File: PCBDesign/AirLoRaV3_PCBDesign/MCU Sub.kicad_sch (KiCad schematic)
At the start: 16 parts, among them SW3 SW_Push, U5 STM32F103C8Tx, Y2 8Mhz

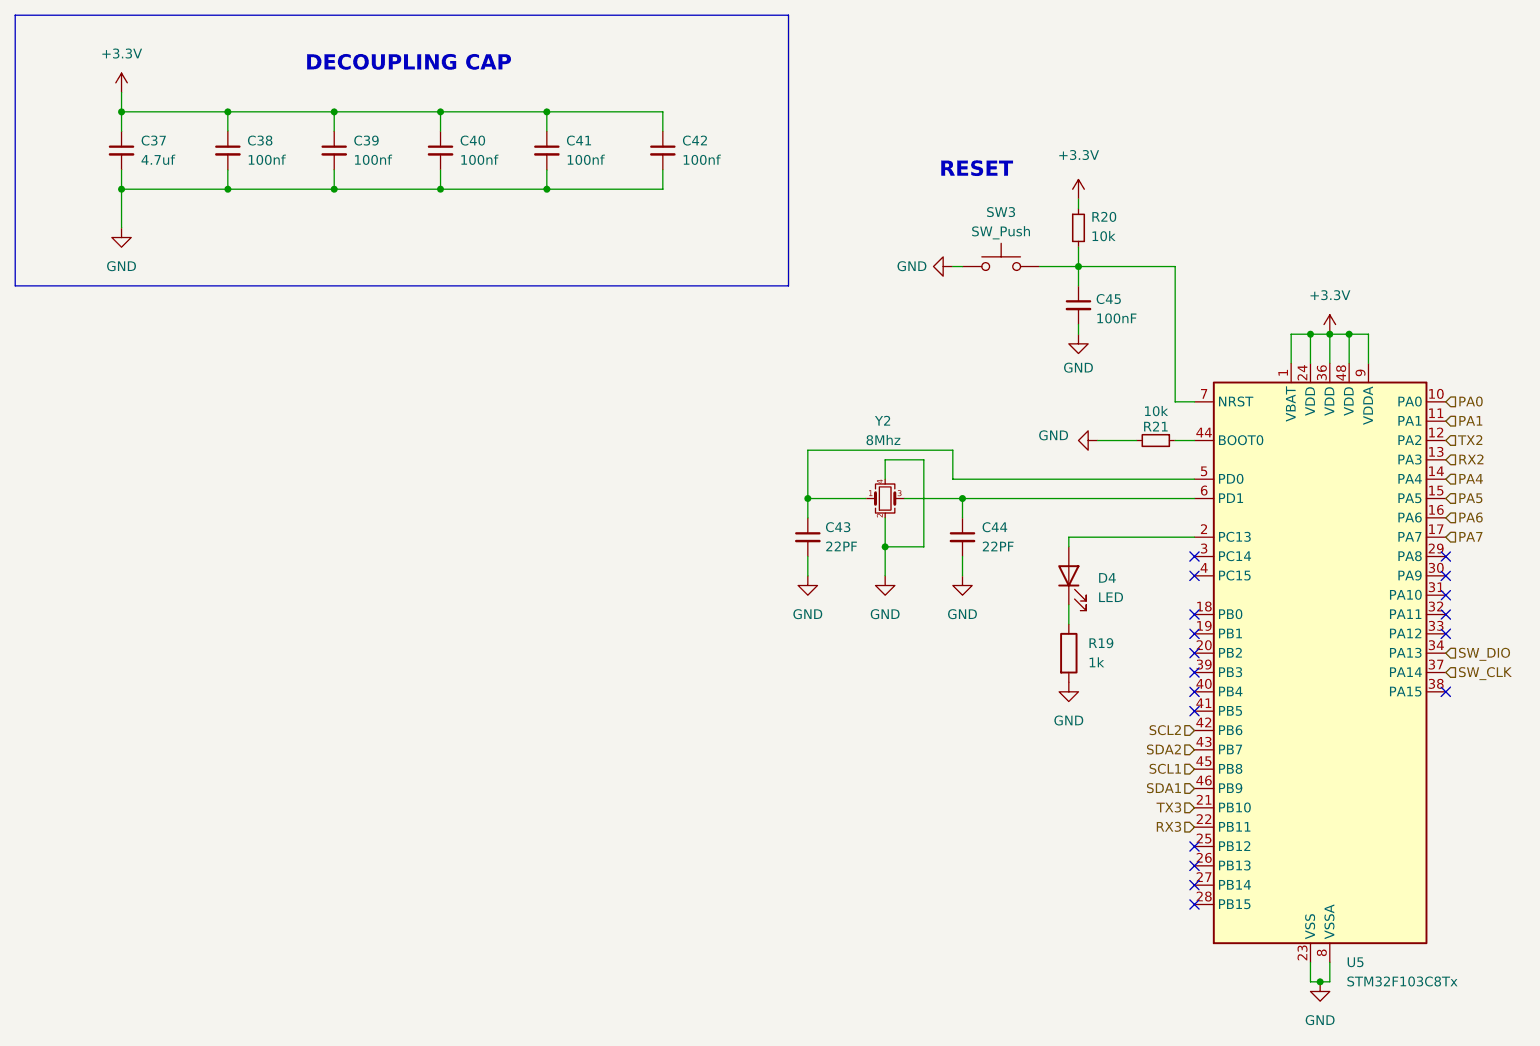
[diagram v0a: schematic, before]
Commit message: Update circuit buck converter and sensor
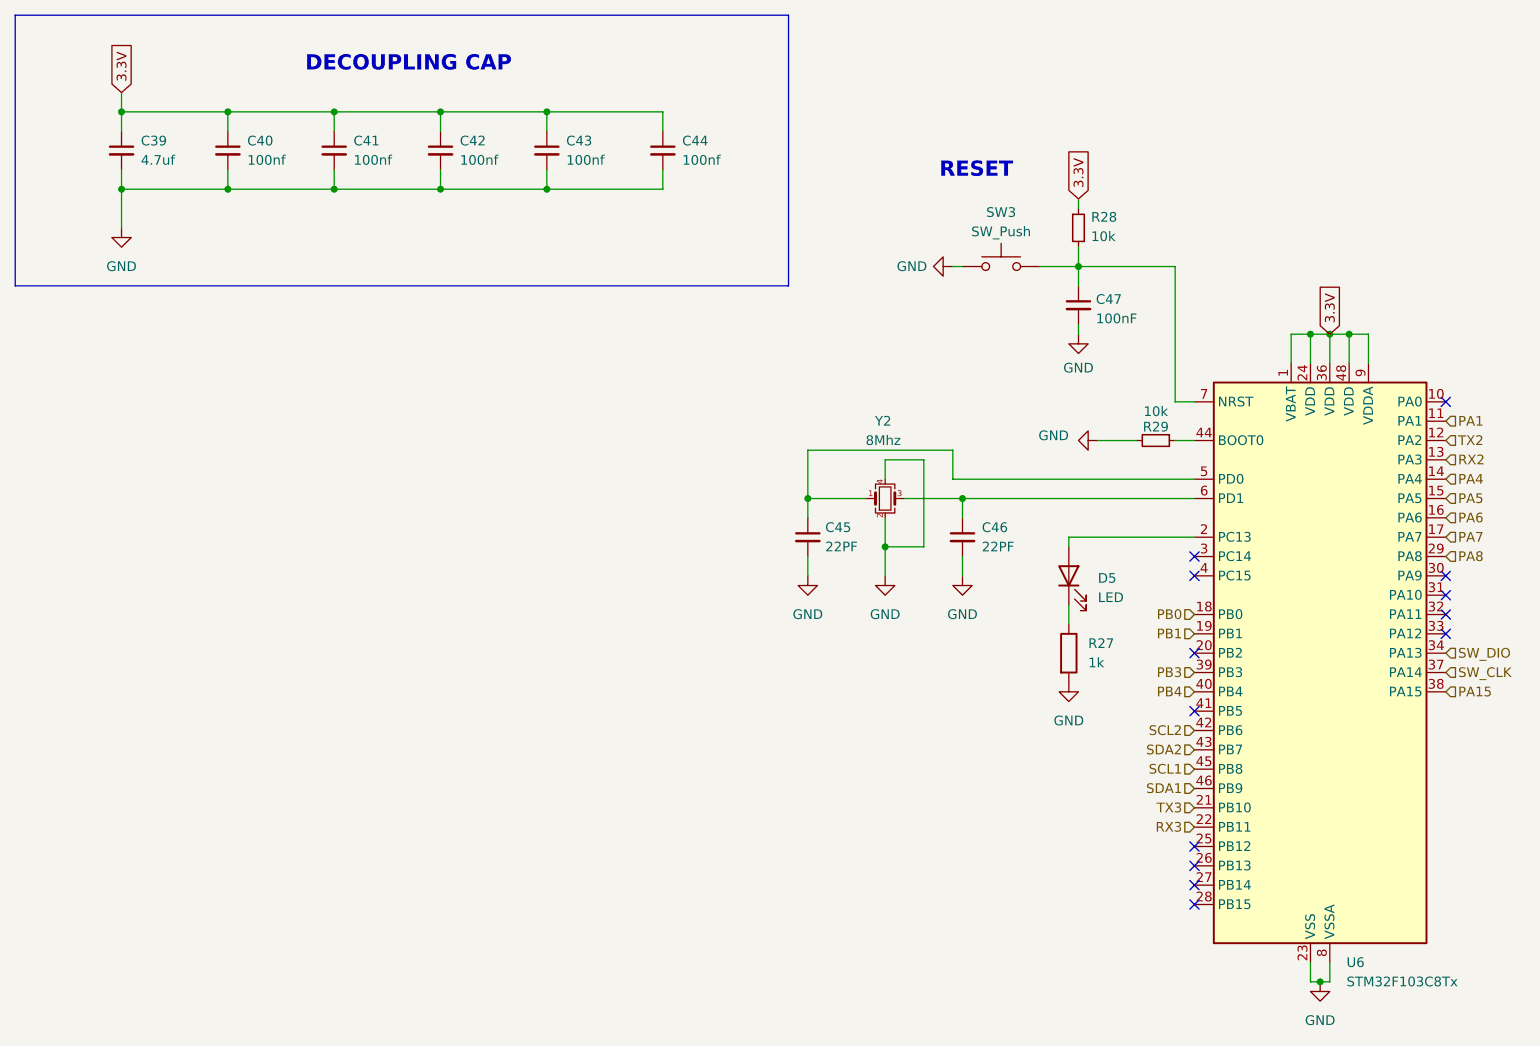
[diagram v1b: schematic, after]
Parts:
- renumbered C37 to C39, C38 to C40, C39 to C41, C40 to C42, C41 to C43, C42 to C44, C43 to C45, C44 to C46, C45 to C47, D4 to D5, R19 to R27, R20 to R28, R21 to R29, U5 to U6
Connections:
- net PB0: now reaches U6.18 (PB0)
- net PB1: now reaches U6.19 (PB1)
- net PA8: now reaches U6.29 (PA8)
- net PA15: now reaches U6.38 (PA15)
- net PB3: now reaches U6.39 (PB3)
- net PB4: now reaches U6.40 (PB4)
- net +3.3V renamed 3.3V
- net PA0: no longer names the net of U6.10 (PA0)
- no-connect marks 18 -> 13

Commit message: Update schematic
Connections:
- net 3.3V renamed +3.3V_HP
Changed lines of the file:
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@@
-		)
-	)
-	(global_label "3.3V"
-		(shape input)
-		(at 29.21 26.67 90)
-		(fields_autoplaced yes)
-		(effects
-			(font
-				(size 1.27 1.27)
-			)
-			(justify left)
-		)
-		(property "Intersheetrefs" "${INTERSHEET_REFS}"
-			(at 29.21 19.5724 90)
-			(effects
-				(font
-					(size 1.27 1.27)
-				)
-				(justify left)
-				(hide yes)
-			)
-		)
-	)
-	(global_label "3.3V"
-		(shape input)
-		(at 187.96 58.42 90)
-		(fields_autoplaced yes)
-		(effects
-			(font
-				(size 1.27 1.27)
-			)
-			(justify left)
-		)
-		(property "Intersheetrefs" "${INTERSHEET_REFS}"
-			(at 187.96 51.3224 90)
-			(effects
-				(font
-					(size 1.27 1.27)
-				)
-				(justify left)
-				(hide yes)
-			)
-		)
-	)
-	(global_label "3.3V"
-		(shape input)
-		(at 154.94 40.64 90)
-		(fields_autoplaced yes)
-		(effects
-			(font
-				(size 1.27 1.27)
-			)
-			(justify left)
-		)
-		(property "Intersheetrefs" "${INTERSHEET_REFS}"
-			(at 154.94 33.5424 90)
-			(effects
-				(font
-					(size 1.27 1.27)
-				)
-				(justify left)
-				(hide yes)
-			)
 		)
 	)
@@
 	)
 	(symbol
+		(lib_id "power:+3.3V")
+		(at 154.94 40.64 0)
+		(unit 1)
+		(exclude_from_sim no)
+		(in_bom yes)
+		(on_board yes)
+		(dnp no)
+		(fields_autoplaced yes)
+		(property "Reference" "#PWR068"
+			(at 154.94 44.45 0)
+			(effects
+				(font
+					(size 1.27 1.27)
+				)
+				(hide yes)
+			)
+		)
+		(property "Value" "+3.3V_HP"
+			(at 154.94 35.56 0)
+			(effects
+				(font
+					(size 1.27 1.27)
+				)
+			)
+		)
+		(property "Footprint" ""
+			(at 154.94 40.64 0)
+			(effects
+				(font
+					(size 1.27 1.27)
+				)
+				(hide yes)
+			)
+		)
+		(property "Datasheet" ""
+			(at 154.94 40.64 0)
+			(effects
+				(font
+					(size 1.27 1.27)
+				)
+				(hide yes)
+			)
+		)
+		(property "Description" "Power symbol creates a global label with name \"+3.3V\""
+			(at 154.94 40.64 0)
+			(effects
+				(font
+					(size 1.27 1.27)
+				)
+				(hide yes)
+			)
+		)
+		(pin "1"
+		)
+		(instances
+			(project "airlora-kicad"
+				(path "/59d971df-d6c1-4ef7-a085-bf08b7b16047/be77b740-d58b-414b-97ce-61f1d1685314/eab4a250-4bd5-4f82-b1cd-88a390e22a6b"
+					(reference "#PWR068")
+					(unit 1)
+				)
+			)
+		)
+	)
+	(symbol
 		(lib_id "power:GND")
 		(at 139.7 90.17 0)
@@
 	)
 	(symbol
+		(lib_id "power:+3.3V")
+		(at 187.96 58.42 0)
+		(unit 1)
+		(exclude_from_sim no)
+		(in_bom yes)
+		(on_board yes)
+		(dnp no)
+		(fields_autoplaced yes)
+		(property "Reference" "#PWR069"
+			(at 187.96 62.23 0)
+			(effects
+				(font
+					(size 1.27 1.27)
+				)
+				(hide yes)
+			)
+		)
+		(property "Value" "+3.3V_HP"
+			(at 187.96 53.34 0)
+			(effects
+				(font
+					(size 1.27 1.27)
+				)
+			)
+		)
+		(property "Footprint" ""
+			(at 187.96 58.42 0)
+			(effects
+				(font
+					(size 1.27 1.27)
+				)
+				(hide yes)
+			)
+		)
+		(property "Datasheet" ""
+			(at 187.96 58.42 0)
+			(effects
+				(font
+					(size 1.27 1.27)
+				)
+				(hide yes)
+			)
+		)
+		(property "Description" "Power symbol creates a global label with name \"+3.3V\""
+			(at 187.96 58.42 0)
+			(effects
+				(font
+					(size 1.27 1.27)
+				)
+				(hide yes)
+			)
+		)
+		(pin "1"
+		)
+		(instances
+			(project "airlora-kicad"
+				(path "/59d971df-d6c1-4ef7-a085-bf08b7b16047/be77b740-d58b-414b-97ce-61f1d1685314/eab4a250-4bd5-4f82-b1cd-88a390e22a6b"
+					(reference "#PWR069")
+					(unit 1)
+				)
+			)
+		)
+	)
+	(symbol
 		(lib_id "Device:C_Small")
 		(at 85.09 34.29 0)
@@
 					(unit 1)
 				)
+			)
+		)
+	)
+	(symbol
+		(lib_id "power:+3.3V")
+		(at 29.21 26.67 0)
+		(unit 1)
+		(exclude_from_sim no)
+		(in_bom yes)
+		(on_board yes)
+		(dnp no)
+		(fields_autoplaced yes)
+		(property "Reference" "#PWR070"
+			(at 29.21 30.48 0)
+			(effects
+				(font
+					(size 1.27 1.27)
+				)
+				(hide yes)
+			)
+		)
+		(property "Value" "+3.3V_HP"
+			(at 29.21 21.59 0)
+			(effects
+				(font
+					(size 1.27 1.27)
+				)
+			)
+		)
+		(property "Footprint" ""
+			(at 29.21 26.67 0)
+			(effects
+				(font
+					(size 1.27 1.27)
+				)
+				(hide yes)
+			)
+		)
+		(property "Datasheet" ""
+			(at 29.21 26.67 0)
+			(effects
+				(font
+					(size 1.27 1.27)
+				)
+				(hide yes)
+			)
+		)
+		(property "Description" "Power symbol creates a global label with name \"+3.3V\""
+			(at 29.21 26.67 0)
+			(effects
+				(font
+					(size 1.27 1.27)
+				)
+				(hide yes)
+			)
+		)
+		(pin "1"
+		)
+		(instances
+			(project "airlora-kicad"
+				(path "/59d971df-d6c1-4ef7-a085-bf08b7b16047/be77b740-d58b-414b-97ce-61f1d1685314/eab4a250-4bd5-4f82-b1cd-88a390e22a6b"
+					(reference "#PWR070")
+					(unit 1)
+				)

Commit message: Update PCB
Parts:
- SW3: footprint Button_Switch_SMD:SW_Push_SPST_NO_Alps_SKRK -> Button_Switch_SMD:SW_Push_1P1T_NO_Vertical_Wuerth_434133025816
- renumbered C39 to C38, C40 to C39, C41 to C40, C42 to C41, C43 to C42, C44 to C43, C45 to C44, C46 to C45, C47 to C46, R27 to R28, R28 to R29, R29 to R30
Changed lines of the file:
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@@
 		(dnp no)
 		(fields_autoplaced yes)
-		(property "Reference" "C46"
+		(property "Reference" "C45"
 			(at 142.24 83.8262 0)
 			(effects
@@
 			(project "airlora-kicad"
 				(path "/59d971df-d6c1-4ef7-a085-bf08b7b16047/be77b740-d58b-414b-97ce-61f1d1685314/eab4a250-4bd5-4f82-b1cd-88a390e22a6b"
-					(reference "C46")
+					(reference "C45")
 					(unit 1)
 				)
@@
 		(on_board yes)
 		(dnp no)
-		(property "Reference" "R29"
+		(property "Reference" "R30"
 			(at 165.1 70.612 90)
 			(effects
@@
 			(project "airlora-kicad"
 				(path "/59d971df-d6c1-4ef7-a085-bf08b7b16047/be77b740-d58b-414b-97ce-61f1d1685314/eab4a250-4bd5-4f82-b1cd-88a390e22a6b"
-					(reference "R29")
+					(reference "R30")
 					(unit 1)
 				)
@@
 		(dnp no)
 		(fields_autoplaced yes)
-		(property "Reference" "#PWR059"
+		(property "Reference" "#PWR068"
 			(at 151.13 72.39 0)
 			(effects
@@
 			(project "airlora-kicad"
 				(path "/59d971df-d6c1-4ef7-a085-bf08b7b16047/be77b740-d58b-414b-97ce-61f1d1685314/eab4a250-4bd5-4f82-b1cd-88a390e22a6b"
-					(reference "#PWR059")
+					(reference "#PWR068")
 					(unit 1)
 				)
@@
 		(dnp no)
 		(fields_autoplaced yes)
-		(property "Reference" "#PWR052"
+		(property "Reference" "#PWR060"
 			(at 29.21 50.8 0)
 			(effects
@@
 			(project "airlora-kicad"
 				(path "/59d971df-d6c1-4ef7-a085-bf08b7b16047/be77b740-d58b-414b-97ce-61f1d1685314/eab4a250-4bd5-4f82-b1cd-88a390e22a6b"
-					(reference "#PWR052")
+					(reference "#PWR060")
 					(unit 1)
 				)
@@
 		(dnp no)
 		(fields_autoplaced yes)
-		(property "Reference" "C39"
+		(property "Reference" "C38"
 			(at 31.75 33.0262 0)
 			(effects
@@
 			(project "airlora-kicad"
 				(path "/59d971df-d6c1-4ef7-a085-bf08b7b16047/be77b740-d58b-414b-97ce-61f1d1685314/eab4a250-4bd5-4f82-b1cd-88a390e22a6b"
-					(reference "C39")
+					(reference "C38")
 					(unit 1)
 				)
@@
 		(dnp no)
 		(fields_autoplaced yes)
-		(property "Reference" "C42"
+		(property "Reference" "C41"
 			(at 73.66 33.0262 0)
 			(effects
@@
 			(project "airlora-kicad"
 				(path "/59d971df-d6c1-4ef7-a085-bf08b7b16047/be77b740-d58b-414b-97ce-61f1d1685314/eab4a250-4bd5-4f82-b1cd-88a390e22a6b"
-					(reference "C42")
+					(reference "C41")
 					(unit 1)
 				)
@@
 		(dnp no)
 		(fields_autoplaced yes)
-		(property "Reference" "#PWR060"
+		(property "Reference" "#PWR069"
 			(at 186.69 149.86 0)
 			(effects
@@
 			(project "airlora-kicad"
 				(path "/59d971df-d6c1-4ef7-a085-bf08b7b16047/be77b740-d58b-414b-97ce-61f1d1685314/eab4a250-4bd5-4f82-b1cd-88a390e22a6b"
-					(reference "#PWR060")
+					(reference "#PWR069")
 					(unit 1)
 				)
@@
 		(dnp no)
 		(fields_autoplaced yes)
-		(property "Reference" "#PWR068"
+		(property "Reference" "#PWR066"
 			(at 154.94 44.45 0)
 			(effects
@@
 			(project "airlora-kicad"
 				(path "/59d971df-d6c1-4ef7-a085-bf08b7b16047/be77b740-d58b-414b-97ce-61f1d1685314/eab4a250-4bd5-4f82-b1cd-88a390e22a6b"
-					(reference "#PWR068")
+					(reference "#PWR066")
 					(unit 1)
 				)
@@
 		(dnp no)
 		(fields_autoplaced yes)
-		(property "Reference" "#PWR056"
+		(property "Reference" "#PWR064"
 			(at 139.7 96.52 0)
 			(effects
@@
 			(project "airlora-kicad"
 				(path "/59d971df-d6c1-4ef7-a085-bf08b7b16047/be77b740-d58b-414b-97ce-61f1d1685314/eab4a250-4bd5-4f82-b1cd-88a390e22a6b"
-					(reference "#PWR056")
+					(reference "#PWR064")
 					(unit 1)
 				)
@@
 		(dnp no)
 		(fields_autoplaced yes)
-		(property "Reference" "C44"
+		(property "Reference" "C43"
 			(at 102.87 33.0262 0)
 			(effects
@@
 			(project "airlora-kicad"
 				(path "/59d971df-d6c1-4ef7-a085-bf08b7b16047/be77b740-d58b-414b-97ce-61f1d1685314/eab4a250-4bd5-4f82-b1cd-88a390e22a6b"
-					(reference "C44")
+					(reference "C43")
 					(unit 1)
 				)
@@
 		(dnp no)
 		(fields_autoplaced yes)
-		(property "Reference" "C40"
+		(property "Reference" "C39"
 			(at 45.72 33.0262 0)
 			(effects
@@
 			(project "airlora-kicad"
 				(path "/59d971df-d6c1-4ef7-a085-bf08b7b16047/be77b740-d58b-414b-97ce-61f1d1685314/eab4a250-4bd5-4f82-b1cd-88a390e22a6b"
-					(reference "C40")
+					(reference "C39")
 					(unit 1)
 				)
@@
 		(on_board yes)
 		(dnp no)
-		(property "Reference" "C47"
+		(property "Reference" "C46"
 			(at 157.226 53.848 0)
 			(effects
@@
 			(project "airlora-kicad"
 				(path "/59d971df-d6c1-4ef7-a085-bf08b7b16047/be77b740-d58b-414b-97ce-61f1d1685314/eab4a250-4bd5-4f82-b1cd-88a390e22a6b"
-					(reference "C47")
+					(reference "C46")
 					(unit 1)
 				)
@@
 		(dnp no)
 		(fields_autoplaced yes)
-		(property "Reference" "#PWR053"
+		(property "Reference" "#PWR061"
 			(at 119.38 96.52 0)
 			(effects
@@
 			(project "airlora-kicad"
 				(path "/59d971df-d6c1-4ef7-a085-bf08b7b16047/be77b740-d58b-414b-97ce-61f1d1685314/eab4a250-4bd5-4f82-b1cd-88a390e22a6b"
-					(reference "#PWR053")
+					(reference "#PWR061")
 					(unit 1)
 				)
@@
 		(dnp no)
 		(fields_autoplaced yes)
-		(property "Reference" "C41"
+		(property "Reference" "C40"
 			(at 59.69 33.0262 0)
 			(effects
@@
 			(project "airlora-kicad"
 				(path "/59d971df-d6c1-4ef7-a085-bf08b7b16047/be77b740-d58b-414b-97ce-61f1d1685314/eab4a250-4bd5-4f82-b1cd-88a390e22a6b"
-					(reference "C41")
+					(reference "C40")
 					(unit 1)
 				)
@@
 		(on_board yes)
 		(dnp no)
-		(property "Reference" "#PWR055"
+		(property "Reference" "#PWR063"
 			(at 132.08 49.53 0)
 			(effects
@@
 			(project "airlora-kicad"
 				(path "/59d971df-d6c1-4ef7-a085-bf08b7b16047/be77b740-d58b-414b-97ce-61f1d1685314/eab4a250-4bd5-4f82-b1cd-88a390e22a6b"
-					(reference "#PWR055")
+					(reference "#PWR063")
 					(unit 1)
 				)
@@
 		(on_board yes)
 		(dnp no)
-		(property "Reference" "C45"
+		(property "Reference" "C44"
 			(at 121.666 83.82 0)
 			(effects
@@
 			(project "airlora-kicad"
 				(path "/59d971df-d6c1-4ef7-a085-bf08b7b16047/be77b740-d58b-414b-97ce-61f1d1685314/eab4a250-4bd5-4f82-b1cd-88a390e22a6b"
-					(reference "C45")
+					(reference "C44")
 					(unit 1)
 				)
@@
 		(dnp no)
 		(fields_autoplaced yes)
-		(property "Reference" "#PWR054"
+		(property "Reference" "#PWR062"
 			(at 129.54 96.52 0)
 			(effects
@@
 			(project "airlora-kicad"
 				(path "/59d971df-d6c1-4ef7-a085-bf08b7b16047/be77b740-d58b-414b-97ce-61f1d1685314/eab4a250-4bd5-4f82-b1cd-88a390e22a6b"
-					(reference "#PWR054")
+					(reference "#PWR062")
 					(unit 1)
 				)
@@
 			)
 		)
-		(property "Footprint" "Button_Switch_SMD:SW_Push_SPST_NO_Alps_SKRK"
+		(property "Footprint" "Button_Switch_SMD:SW_Push_1P1T_NO_Vertical_Wuerth_434133025816"
 			(at 144.78 44.45 0)
 			(effects
@@
 		(dnp no)
 		(fields_autoplaced yes)
-		(property "Reference" "#PWR069"
+		(property "Reference" "#PWR070"
 			(at 187.96 62.23 0)
 			(effects
@@
 			(project "airlora-kicad"
 				(path "/59d971df-d6c1-4ef7-a085-bf08b7b16047/be77b740-d58b-414b-97ce-61f1d1685314/eab4a250-4bd5-4f82-b1cd-88a390e22a6b"
-					(reference "#PWR069")
+					(reference "#PWR070")
 					(unit 1)
 				)
@@
 		(dnp no)
 		(fields_autoplaced yes)
-		(property "Reference" "C43"
+		(property "Reference" "C42"
 			(at 87.63 33.0262 0)
 			(effects
@@
 			(project "airlora-kicad"
 				(path "/59d971df-d6c1-4ef7-a085-bf08b7b16047/be77b740-d58b-414b-97ce-61f1d1685314/eab4a250-4bd5-4f82-b1cd-88a390e22a6b"
-					(reference "C43")
+					(reference "C42")
 					(unit 1)
 				)
@@
 		(on_board yes)
 		(dnp no)
-		(property "Reference" "R28"
+		(property "Reference" "R29"
 			(at 156.591 43.053 0)
 			(effects
@@
 			(project "airlora-kicad"
 				(path "/59d971df-d6c1-4ef7-a085-bf08b7b16047/be77b740-d58b-414b-97ce-61f1d1685314/eab4a250-4bd5-4f82-b1cd-88a390e22a6b"
-					(reference "R28")
+					(reference "R29")
 					(unit 1)
 				)
@@
 		(dnp no)
 		(fields_autoplaced yes)
-		(property "Reference" "#PWR070"
+		(property "Reference" "#PWR059"
 			(at 29.21 30.48 0)
 			(effects
@@
 			(project "airlora-kicad"
 				(path "/59d971df-d6c1-4ef7-a085-bf08b7b16047/be77b740-d58b-414b-97ce-61f1d1685314/eab4a250-4bd5-4f82-b1cd-88a390e22a6b"
-					(reference "#PWR070")
+					(reference "#PWR059")
 					(unit 1)
 				)
@@
 		(dnp no)
 		(fields_autoplaced yes)
-		(property "Reference" "R27"
+		(property "Reference" "R28"
 			(at 156.21 99.0599 0)
 			(effects
@@
 			(project "airlora-kicad"
 				(path "/59d971df-d6c1-4ef7-a085-bf08b7b16047/be77b740-d58b-414b-97ce-61f1d1685314/eab4a250-4bd5-4f82-b1cd-88a390e22a6b"
-					(reference "R27")
+					(reference "R28")
 					(unit 1)
 				)
@@
 		(dnp no)
 		(fields_autoplaced yes)
-		(property "Reference" "#PWR057"
+		(property "Reference" "#PWR065"
 			(at 153.67 110.49 0)
 			(effects
@@
 			(project "airlora-kicad"
 				(path "/59d971df-d6c1-4ef7-a085-bf08b7b16047/be77b740-d58b-414b-97ce-61f1d1685314/eab4a250-4bd5-4f82-b1cd-88a390e22a6b"
-					(reference "#PWR057")
+					(reference "#PWR065")
 					(unit 1)
 				)
@@
 		(dnp no)
 		(fields_autoplaced yes)
-		(property "Reference" "#PWR058"
+		(property "Reference" "#PWR067"
 			(at 154.94 64.77 0)
 			(effects
@@
 			(project "airlora-kicad"
 				(path "/59d971df-d6c1-4ef7-a085-bf08b7b16047/be77b740-d58b-414b-97ce-61f1d1685314/eab4a250-4bd5-4f82-b1cd-88a390e22a6b"
-					(reference "#PWR058")
-					(unit 1)
-				)
+					(reference "#PWR067")
+					(unit 1)
+				)
